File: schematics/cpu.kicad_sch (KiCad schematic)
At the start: 12 parts, among them U8 W65C02SxP

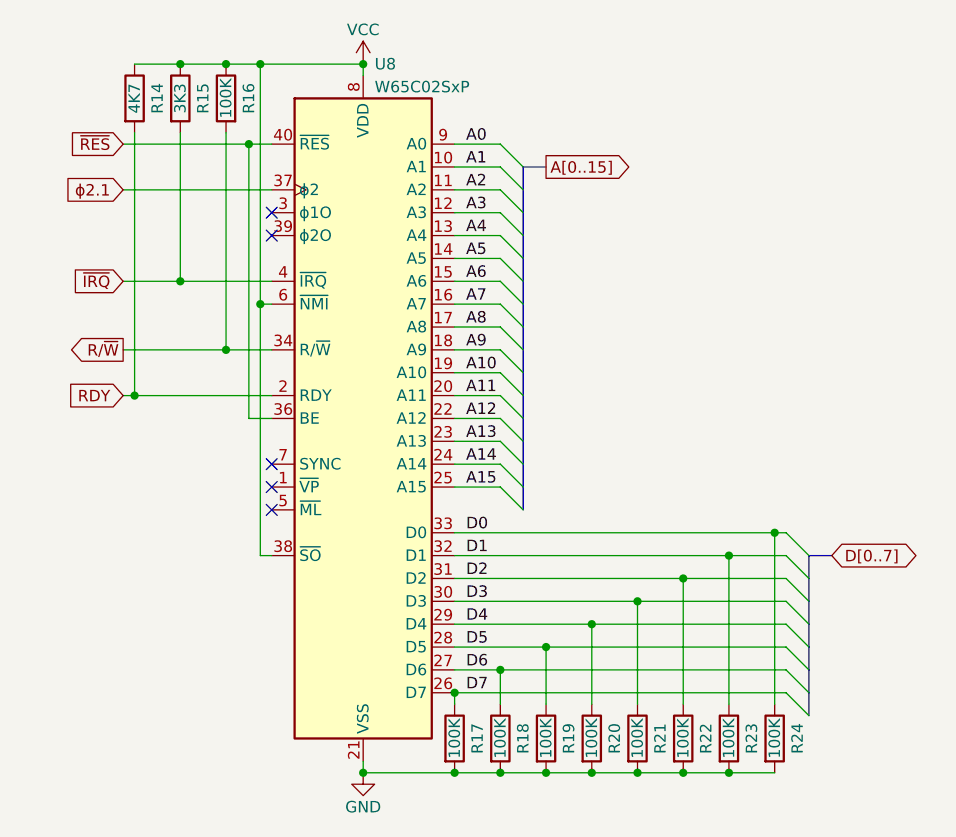
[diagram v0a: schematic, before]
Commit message: new ft245 support
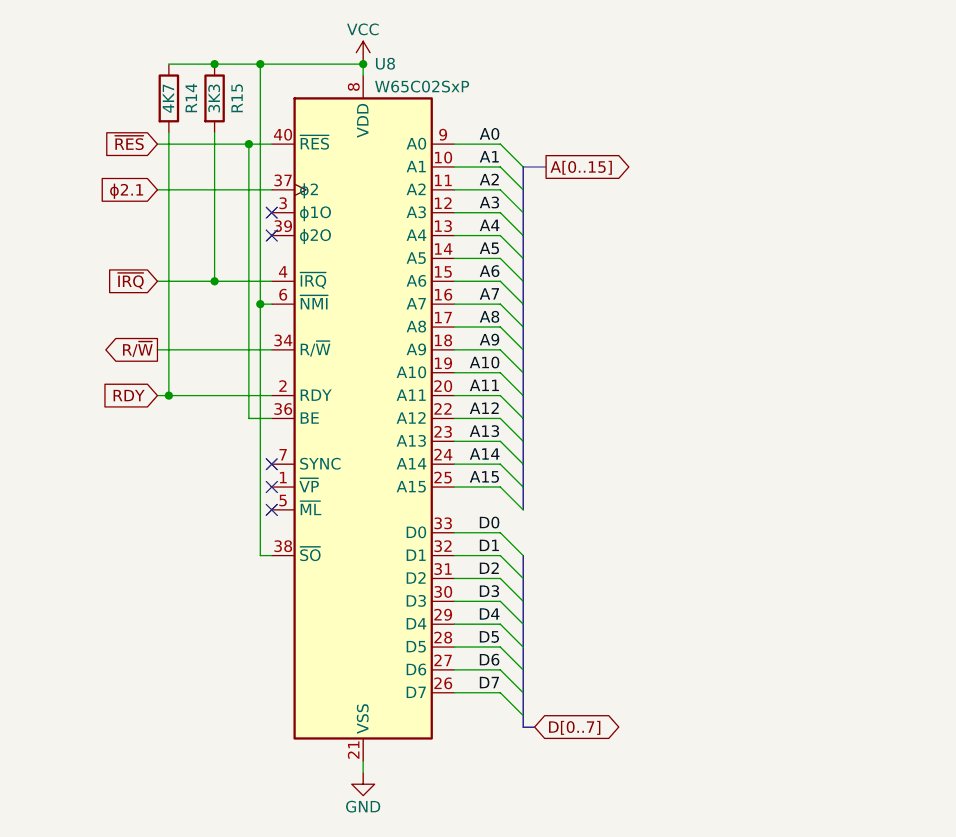
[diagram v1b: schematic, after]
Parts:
- removed R16, R17, R18, R19, R20, R21, R22, R23, R24: 100K, symbol Device:R
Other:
- moved on the sheet: R14, R15
